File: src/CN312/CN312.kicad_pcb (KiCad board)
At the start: 2 copper layers, 21.5 x 10 mm, 9 parts, among them J1 in, J2 out, Q1 NMOS, U1 CN312

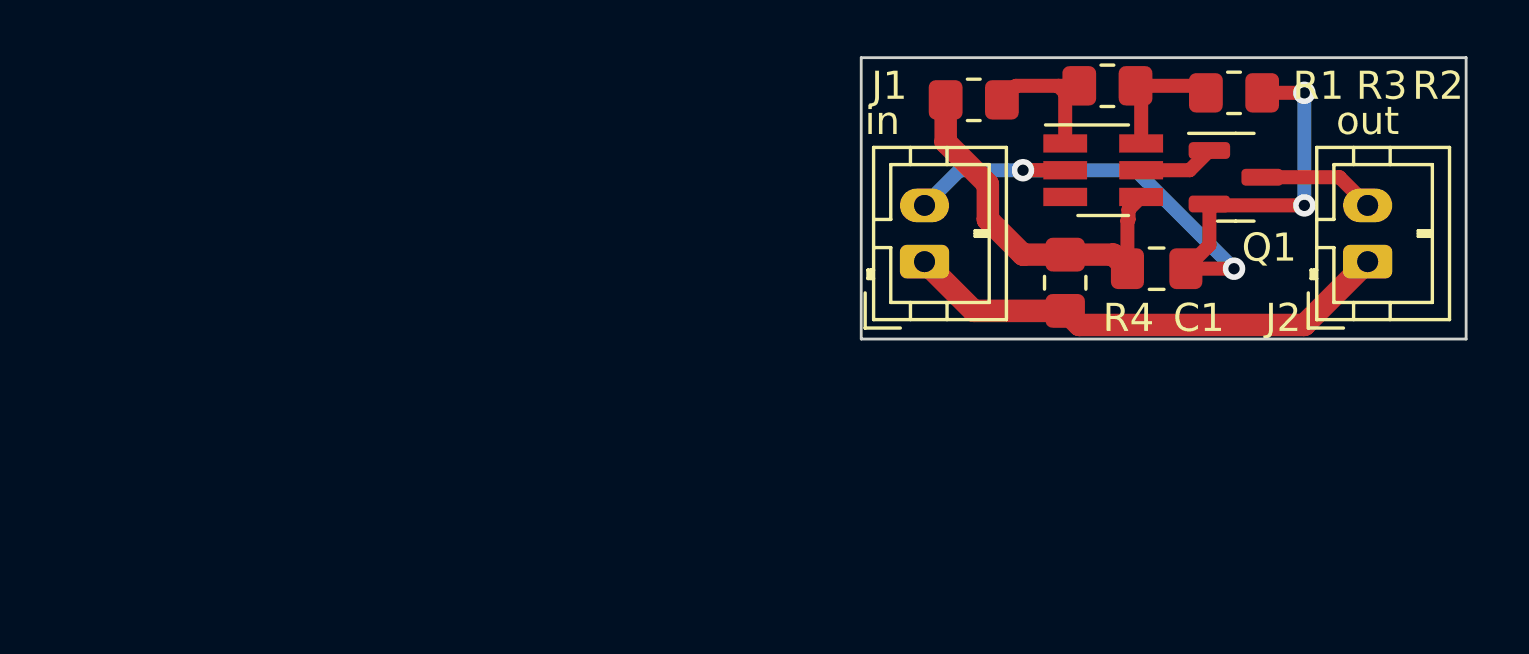
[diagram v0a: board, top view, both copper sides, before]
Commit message: Add files via upload
PH2.0 的所在附近不要這麼大片的舖銅比較好，以防止意外造成短路。 (感謝周喬治大的貢獻)
Reduce copper pour area near PH2.0 to prevent accidental shorts. (Thanks to George Chou)
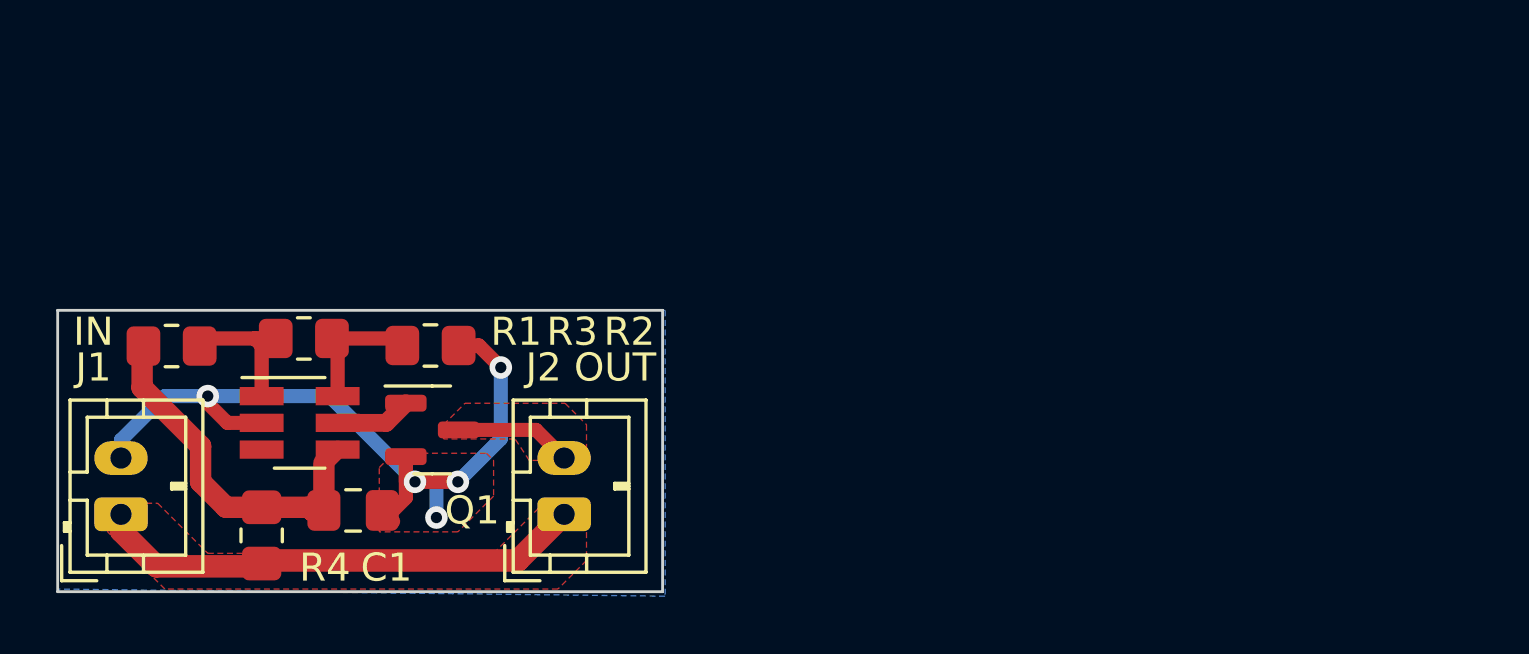
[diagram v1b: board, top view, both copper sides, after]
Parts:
- J1: value in -> IN
- J2: value out -> OUT
- moved J1 29.9 mm to (93.7, 101.2)
- moved J2 29.9 mm to (109.4, 101.2)
- moved Q1 29.9 mm to (104.8, 98.2)
- moved R2 29.9 mm to (104.7, 95.2)
- moved R3 29.9 mm to (100.2, 95.0)
- moved R4 29.9 mm to (98.7, 102.0)
- moved U1 29.9 mm to (100.0, 98.0)
- moved R1 29.8 mm to (95.5, 95.2)
- moved C1 29.8 mm to (101.9, 101.1)
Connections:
- J1 pad 1: Net-(J1-P$1) -> Net-(J2-P$2)
- J2 pad 1: Net-(J1-P$1) -> Net-(J2-P$2)
- R4 pad 1: Net-(J1-P$1) -> Net-(J2-P$2)
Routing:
- net Net-(J2-P$2): track 4.16 -> 21.8 mm
- net Net-(J1-P$1): track 17.6 -> 0.00 mm
- net GND: track 27.7 -> 31.3 mm, vias 4 -> 5
- net Net-(U1-FTH): track 5.11 -> 5.86 mm
- net Net-(U1-VCC): track 13.3 -> 12.6 mm
- added copper zone on F.Cu, net Net-(J2-P$2)
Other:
- board text added: "Vin"
- board text added: "Vout"
- board text removed: "V+"
